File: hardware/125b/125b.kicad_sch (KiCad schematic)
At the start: 48 parts, among them J1 Guitar in, J2 Barrel_Jack, J3 Conn_02x05_Odd_Even_MountingP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, J4 Guitar out, SW2 RotaryEncoder_Switch, SW3 SW_Push, SW4 SW_Push, U1 L78L05_TO92, U2 TL074

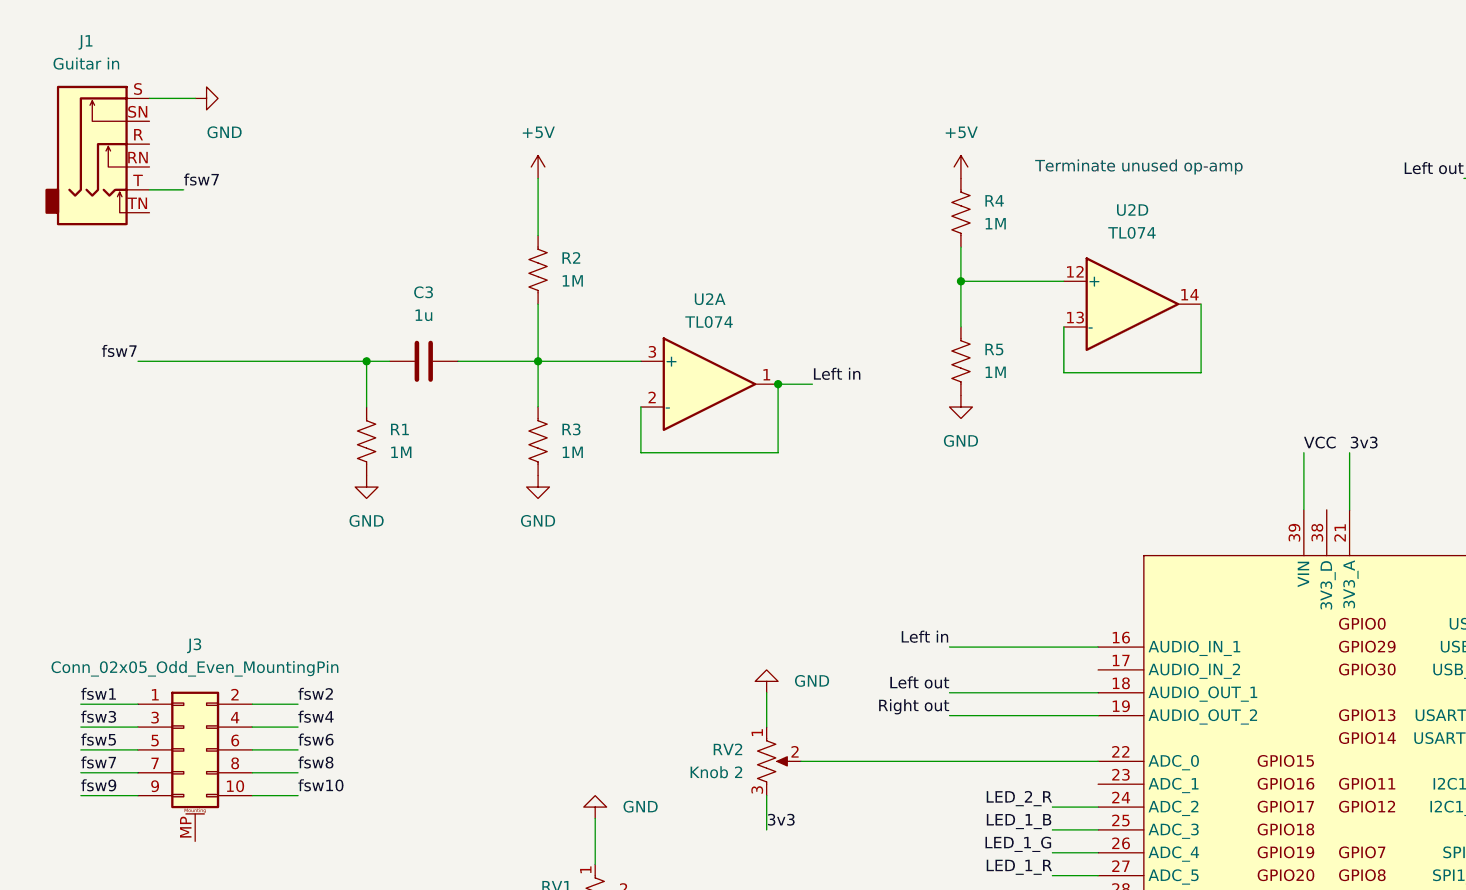
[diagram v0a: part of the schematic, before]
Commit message: Add stereo input to schematic and start pcb changes
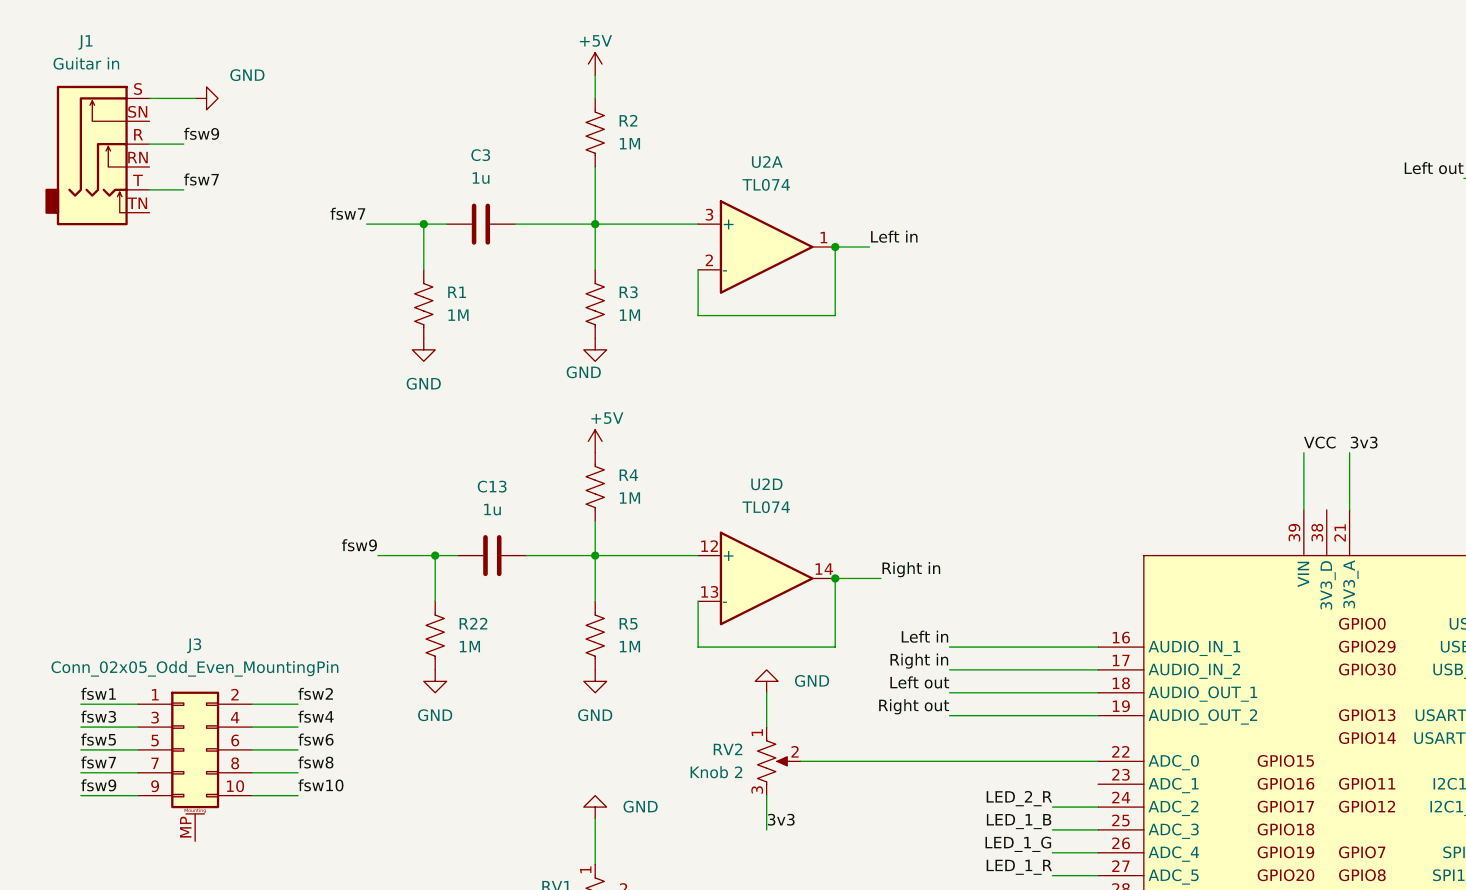
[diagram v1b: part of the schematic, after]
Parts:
- added C13: 1u, Capacitor_SMD:C_0805_2012Metric, symbol Device:C
- added R22: 1M, Resistor_SMD:R_0805_2012Metric, symbol Device:R_US
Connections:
- net GND: now also R22.2
- net fsw9: now also J1.R, C13.1, R22.1
- net at R4.2, R5.1, U2.12 (+): now also C13.2
- net Right in: now reaches U2.13 (-), U2.14
- net Right in: now also A1.17 (AUDIO_IN_2)
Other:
- note removed: "Terminate unused op-amp"
- moved on the sheet: C3, R1, R2, R3, R4, R5, U2A, U2D
